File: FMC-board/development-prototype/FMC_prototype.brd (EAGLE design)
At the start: 103.8 x 69.8 mm, 72 parts, among them J1 DC_POWER_JACK-PJ-102AH, J2 DC_POWER_JACK-PJ-102AH

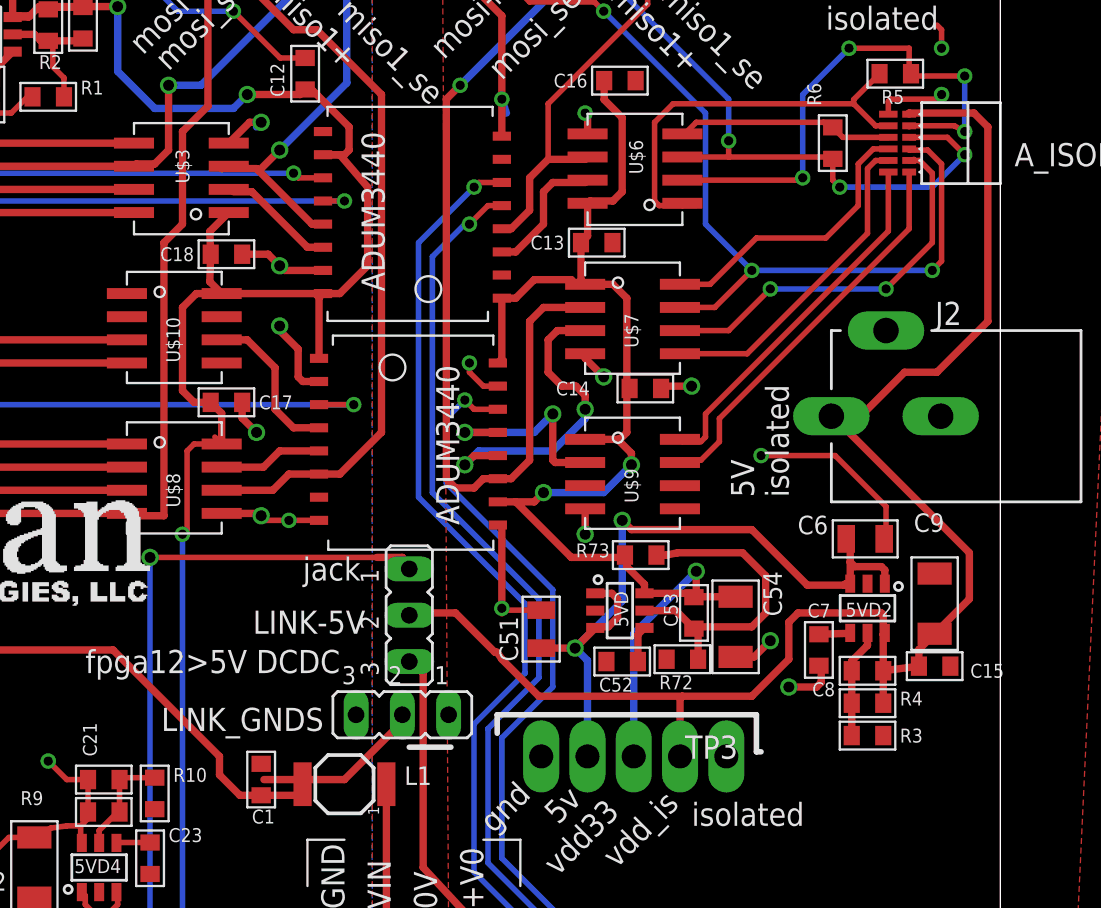
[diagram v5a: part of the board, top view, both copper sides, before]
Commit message: Fixed small routing error on DC DC converter
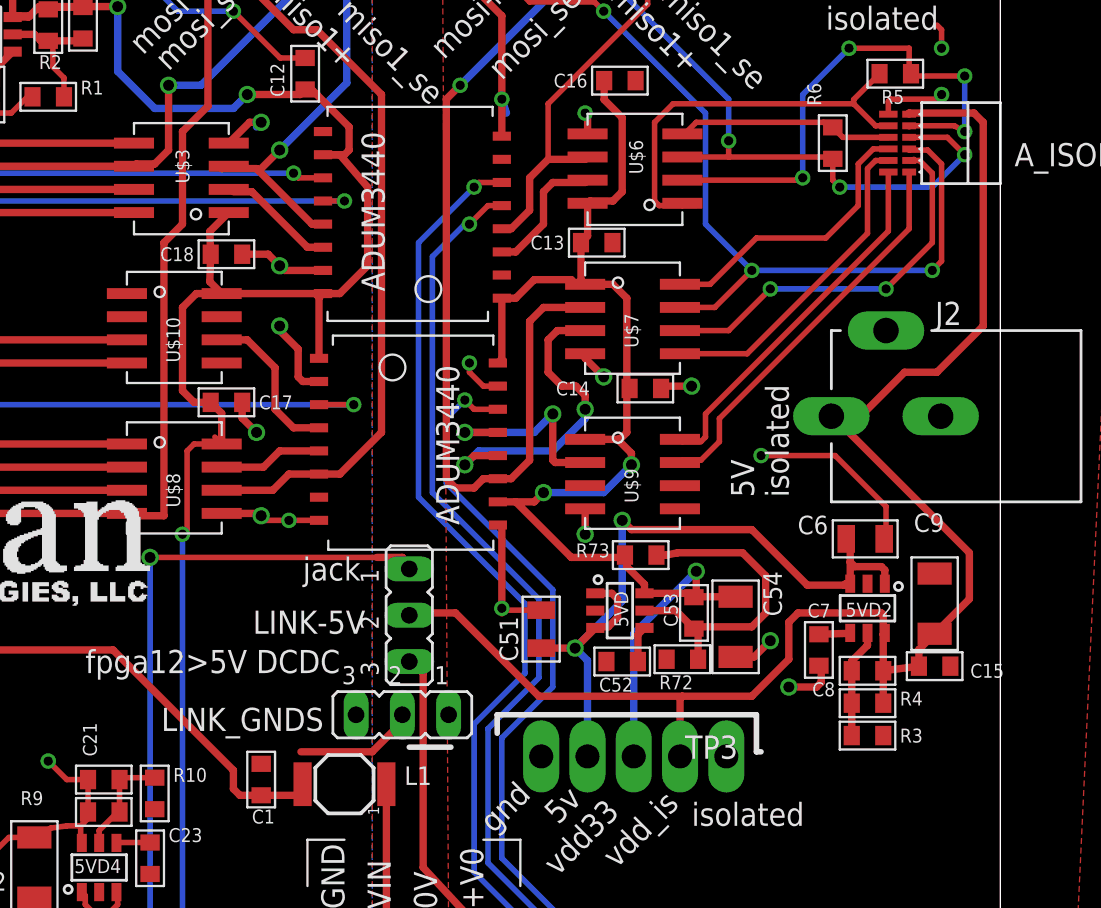
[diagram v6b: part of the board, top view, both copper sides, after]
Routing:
- net GND: track 104.7 -> 102.0 mm
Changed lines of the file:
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@@
 <grid distance="0.01" unitdist="inch" unit="inch" style="lines" multiple="1" display="yes" altdistance="0.0125" altunitdist="inch" altunit="inch"/>
 <layers>
-<layer number="1" name="Top" color="12" fill="1" visible="no" active="yes"/>
+<layer number="1" name="Top" color="12" fill="1" visible="yes" active="yes"/>
 <layer number="2" name="$GND" color="2" fill="1" visible="no" active="yes"/>
 <layer number="3" name="Route3" color="4" fill="3" visible="no" active="no"/>
@@
 <contactref element="U$20" pad="P1"/>
 <wire x1="70.993" y1="25.146" x2="70.993" y2="24.765" width="0.4064" layer="1"/>
-<wire x1="70.993" y1="24.765" x2="67.818" y2="21.59" width="0.4064" layer="1"/>
-<wire x1="67.818" y1="21.59" x2="63.3984" y2="21.59" width="0.4064" layer="1"/>
+<wire x1="70.993" y1="24.765" x2="69.342" y2="23.114" width="0.4064" layer="1"/>
+<wire x1="69.342" y1="23.114" x2="65.4304" y2="23.114" width="0.4064" layer="1"/>
 <wire x1="15.24" y1="57.15" x2="15.24" y2="54.61" width="0" layer="19" extent="16-16"/>
 <wire x1="21.59" y1="35.56" x2="21.59" y2="39.37" width="0" layer="19" extent="16-16"/>
@@
 <wire x1="90.17" y1="26.162" x2="86.36" y2="26.162" width="0.4064" layer="1"/>
 <wire x1="86.36" y1="26.162" x2="78.486" y2="26.162" width="0.4064" layer="1"/>
-<wire x1="78.486" y1="26.162" x2="76.454" y2="28.194" width="0.4064" layer="1"/>
-<wire x1="76.454" y1="28.194" x2="76.2" y2="28.575" width="0.4064" layer="1"/>
 <wire x1="94.536" y1="41.529" x2="94.615" y2="41.529" width="0.4064" layer="1"/>
 <wire x1="94.615" y1="41.529" x2="102.108" y2="34.036" width="0.4064" layer="1"/>
@@
 <wire x1="96.139" y1="41.529" x2="98.552" y2="43.942" width="0.4064" layer="1"/>
 <wire x1="98.552" y1="43.942" x2="100.33" y2="43.942" width="0.4064" layer="1"/>
-<wire x1="100.33" y1="43.942" x2="103.124" y2="46.736" width="0.4064" layer="1"/>
-<wire x1="103.124" y1="46.736" x2="103.124" y2="57.404" width="0.4064" layer="1"/>
-<wire x1="103.124" y1="57.404" x2="102.362" y2="58.166" width="0.4064" layer="1"/>
+<wire x1="100.33" y1="43.942" x2="102.87" y2="46.482" width="0.4064" layer="1"/>
+<wire x1="102.87" y1="46.482" x2="102.87" y2="57.658" width="0.4064" layer="1"/>
+<wire x1="102.87" y1="57.658" x2="102.362" y2="58.166" width="0.4064" layer="1"/>
 <wire x1="102.362" y1="58.166" x2="98.806" y2="58.166" width="0.4064" layer="1"/>
 <wire x1="98.806" y1="58.166" x2="98.806" y2="58.1025" width="0.4064" layer="1"/>
@@
 <wire x1="86.233" y1="26.035" x2="86.36" y2="26.162" width="0.4064" layer="1"/>
 <contactref element="LINK-5V" pad="2"/>
-<wire x1="76.2" y1="28.575" x2="76.073" y2="28.575" width="0.4064" layer="1"/>
-<wire x1="76.073" y1="28.575" x2="73.914" y2="30.734" width="0.4064" layer="1"/>
 <wire x1="73.914" y1="30.734" x2="71.501" y2="30.734" width="0.4064" layer="1"/>
 <wire x1="71.501" y1="30.734" x2="71.374" y2="30.607" width="0.4064" layer="1"/>
+<wire x1="78.486" y1="26.162" x2="73.914" y2="30.734" width="0.4064" layer="1"/>
 </signal>
 <signal name="VDD33">
@@
 <wire x1="65.518" y1="21.096" x2="65.532" y2="21.082" width="0.4064" layer="1"/>
 <wire x1="63.246" y1="20.7264" x2="62.0776" y2="20.7264" width="0.4064" layer="1"/>
-<wire x1="62.0776" y1="20.7264" x2="60.96" y2="21.844" width="0.4064" layer="1"/>
-<wire x1="60.96" y1="21.844" x2="60.96" y2="22.86" width="0.4064" layer="1"/>
-<wire x1="60.96" y1="22.86" x2="55.118" y2="28.702" width="0.4064" layer="1"/>
+<wire x1="62.0776" y1="20.7264" x2="61.722" y2="21.082" width="0.4064" layer="1"/>
+<wire x1="61.722" y1="21.082" x2="61.722" y2="22.098" width="0.4064" layer="1"/>
+<wire x1="61.722" y1="22.098" x2="55.118" y2="28.702" width="0.4064" layer="1"/>
 <wire x1="55.118" y1="28.702" x2="43.688" y2="28.702" width="0.4064" layer="1"/>
 <wire x1="43.688" y1="28.702" x2="42.164" y2="30.226" width="0.4064" layer="1"/>

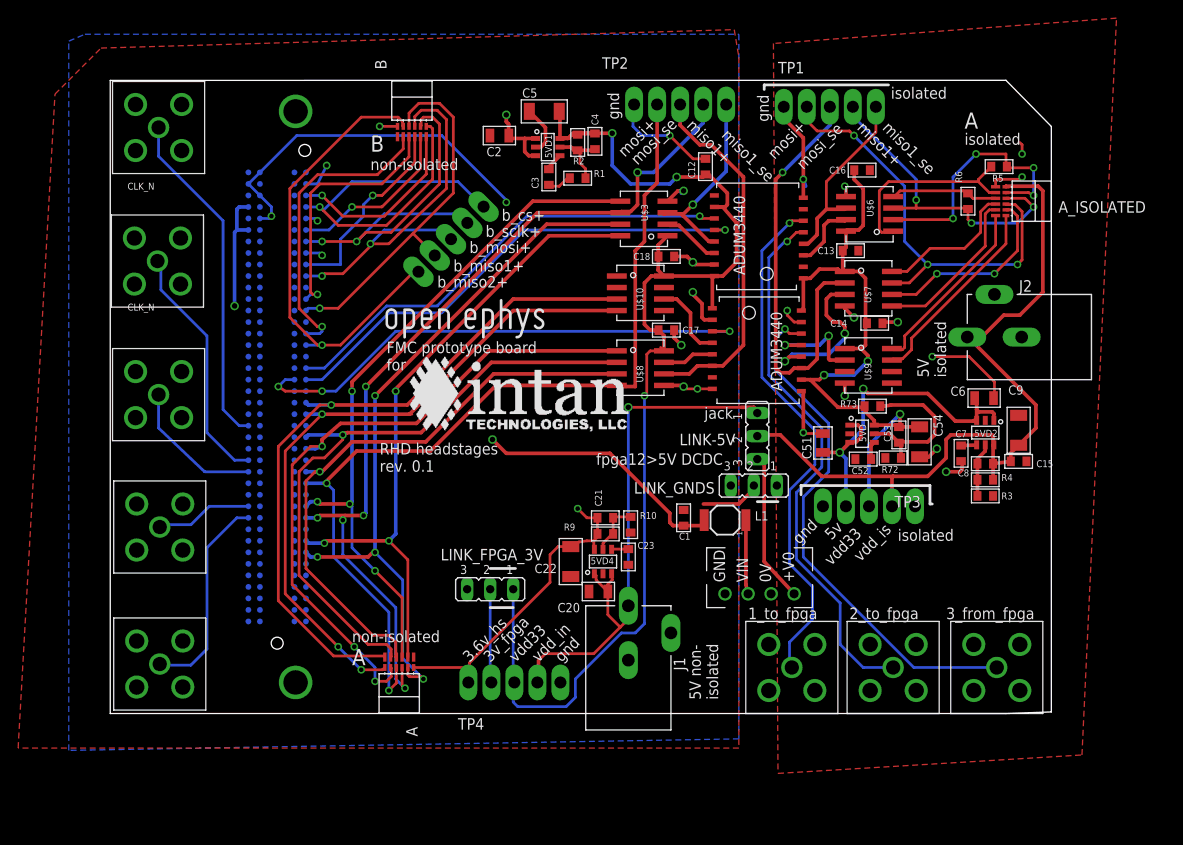
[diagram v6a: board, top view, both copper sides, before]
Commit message: Cleaning up schematic as a means to understand and verify it.
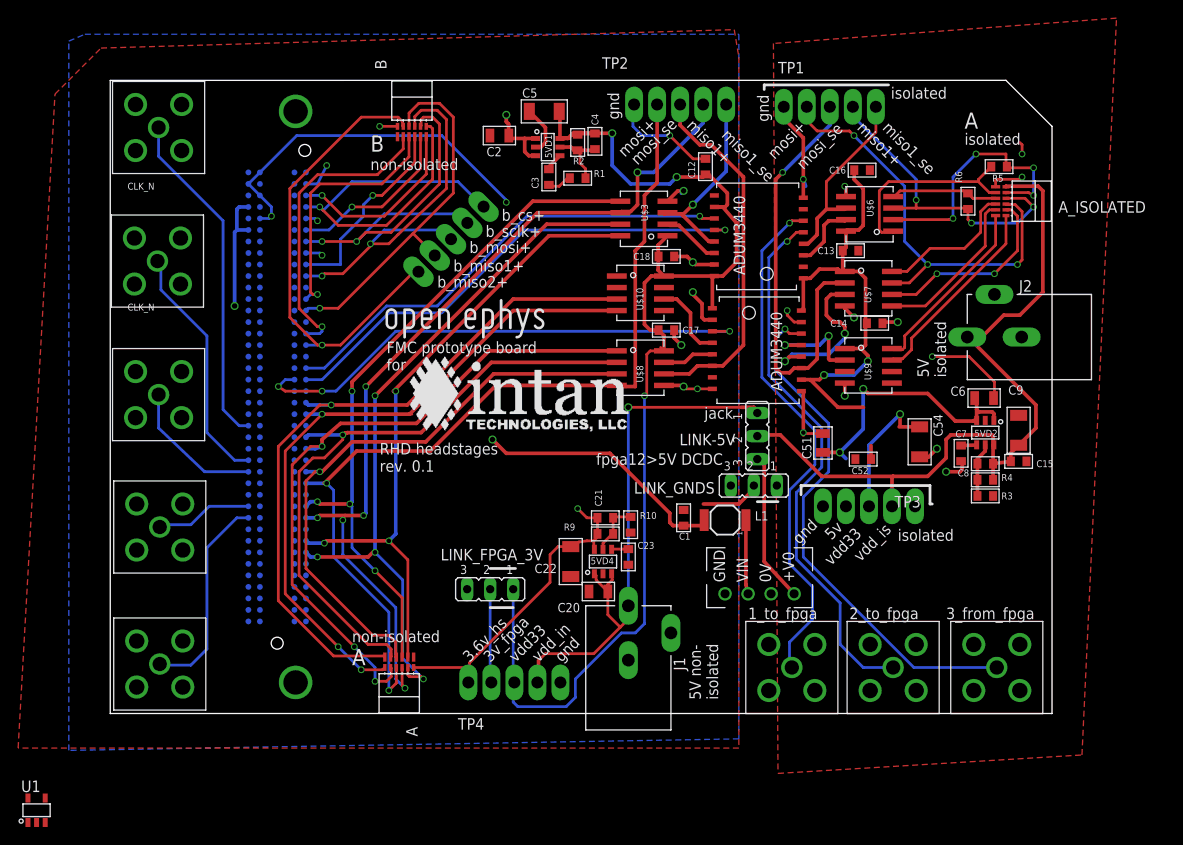
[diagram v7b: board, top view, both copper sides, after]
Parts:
- removed 5VD: TPS79301, RHD2000_eval_board:SOT-23-6
- removed C53: 15p, RHD2000_eval_board:0603
- removed R72: 30.9k, RHD2000_eval_board:0603
- removed R73: 95.3k, RHD2000_eval_board:0603
- added U1: TPS79333, jonnew:SOT-23-5
- J2: value DC_POWER_JACK-PJ-102AH -> PJ-102AH
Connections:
- net VDD33 renamed +3V3
- net VDD36 renamed +3V6
- net VDD_ISOLATED renamed VDD_ISO
- removed net GND_ISOLATED: 5VD.2, 5VD2.2, A_ISOLATED.T6, C13.2, C14.2, C15.2, C16.2, C51.2, C52.2, C54.2, C6.2, C7.2, C9.2, J2.2, J2.3, LINK_GNDS.1, R3.2, R72.2, TP1.TP-1, TP3.TP-1, TP3.TP-5, U$11.P2, U$11.P8, U$12.P15, U$12.P9, U$17.GND$1, U$17.GND$2, U$17.GND$3, U$17.GND$4, U$18.GND$1, U$18.GND$2, U$18.GND$3, U$18.GND$4, U$19.GND$1, U$19.GND$2, U$19.GND$3, U$19.GND$4, U$20.P3, U$6.P5, U$7.P4, U$9.P4
- removed net N$108: 5VD.5, C53.2, R72.1, R73.1
- removed net N$3: LINK_FPGA_3V.3
- removed net VDD33_ISOLATED: 5VD.6, C13.1, C14.1, C16.1, C53.1, C54.1, R73.2, TP3.TP-3, U$11.P1, U$12.P10, U$12.P16, U$6.P8, U$7.P1, U$9.P1
- new net 5V_ISO: TP3.TP-4
- new net GND_ISO: 5VD2.2, A_ISOLATED.T6, C13.2, C14.2, C15.2, C16.2, C51.2, C52.2, C54.2, C6.2, C7.2, C9.2, J2.2, J2.3, LINK_GNDS.1, R3.2, TP1.TP-1, TP3.TP-1, TP3.TP-5, U$11.P2, U$11.P8, U$12.P15, U$12.P9, U$17.GND$1, U$17.GND$2, U$17.GND$3, U$17.GND$4, U$18.GND$1, U$18.GND$2, U$18.GND$3, U$18.GND$4, U$19.GND$1, U$19.GND$2, U$19.GND$3, U$19.GND$4, U$20.P3, U$6.P5, U$7.P4, U$9.P4, U1.2
- new net VDD33_ISO: C13.1, C14.1, C16.1, C54.1, TP3.TP-3, U$11.P1, U$12.P10, U$12.P16, U$6.P8, U$7.P1, U$9.P1, U1.5
- net 5V_ISOLATED: now also U1.1, U1.3; no longer 5VD.1, 5VD.3, TP3.TP-4
- net GND: now also U$4.P$6
- net N$97: now also U1.4; no longer 5VD.4
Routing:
- net VDD33_ISOLATED: track 72.0 -> 0.00 mm, vias 3 -> 0
- net VDD33_ISO: track 0.00 -> 66.3 mm, vias 0 -> 3
- net GND_ISOLATED: track 48.6 -> 0.00 mm, vias 12 -> 0
- net GND_ISO: track 0.00 -> 48.6 mm, vias 0 -> 12
- net N$108: track 17.8 -> 0.00 mm
- net 5V_ISOLATED: track 41.0 -> 30.3 mm
- net N$97: track 1.99 -> 1.48 mm
- added copper zone on layer 1, net GND_ISO
- added copper zone on layer 2, net GND_ISO
- removed copper zone on layer 1, net GND_ISOLATED
- removed copper zone on layer 2, net GND_ISOLATED
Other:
- board size 103.8 x 69.8 mm -> 103.9 x 69.8 mm

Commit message: Looks like isolated 5V was wired to output of isolated 3.6V regulator and input is floating to both isolated regulators. In the middle of fixing that.
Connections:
- removed net VDD_ISO: 5VD2.6, A_ISOLATED.B6, C15.1, C8.1, C9.1, J2.1, LINK-5V.2, R4.2, TP3.TP-2
- new net +3V6_ISO: 5VD2.6, A_ISOLATED.B6, C15.1, C8.1, C9.1, R4.2, TP3.TP-2
- new net N$3: C51.2, C52.2, C54.2, U1.2
- new net N$4: J2.2, J2.3, LINK_GNDS.1
- new net N$5: J2.1, LINK-5V.2
- net GND_ISO: no longer C51.2, C52.2, C54.2, J2.2, J2.3, LINK_GNDS.1, U1.2
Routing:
- net VDD_ISO: track 85.2 -> 0.00 mm
- net +3V6_ISO: track 0.00 -> 85.0 mm
- net GND_ISO: track 48.6 -> 44.1 mm, vias 12 -> 10
- net N$3: track 0.00 -> 4.47 mm, vias 0 -> 2
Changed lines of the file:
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@@
 <contactref element="C14" pad="2"/>
 <contactref element="C13" pad="2"/>
-<contactref element="C51" pad="2"/>
-<contactref element="C52" pad="2"/>
-<contactref element="C54" pad="2"/>
 <contactref element="5VD2" pad="2"/>
 <contactref element="C6" pad="2"/>
@@
 <contactref element="TP1" pad="TP-1"/>
 <contactref element="TP3" pad="TP-1"/>
-<contactref element="J2" pad="3"/>
-<contactref element="J2" pad="2"/>
-<contactref element="LINK_GNDS" pad="1"/>
 <polygon width="0.4064" layer="1">
 <vertex x="73.152" y="73.914"/>
@@
 <wire x1="86.868" y1="43.18" x2="85.3186" y2="43.18" width="0.4064" layer="1"/>
 <wire x1="85.3186" y1="43.18" x2="85.1916" y2="43.053" width="0.4064" layer="1"/>
-<wire x1="89.281" y1="28.321" x2="90.297" y2="28.321" width="0.4064" layer="1"/>
-<wire x1="90.297" y1="28.321" x2="91.186" y2="29.21" width="0.4064" layer="1"/>
-<via x="91.186" y="29.21" extent="1-16" drill="0.6"/>
 <via x="92.202" y="26.67" extent="1-16" drill="0.6"/>
 <wire x1="92.202" y1="26.67" x2="93.726" y2="26.67" width="0.4064" layer="1"/>
@@
 <wire x1="97.536" y1="36.576" x2="97.536" y2="34.8996" width="0.3048" layer="1"/>
 <wire x1="97.536" y1="34.8996" x2="97.4344" y2="34.798" width="0.3048" layer="1"/>
-<wire x1="78.613" y1="30.8864" x2="76.5556" y2="30.8864" width="0.3048" layer="1"/>
-<wire x1="76.5556" y1="30.8864" x2="76.454" y2="30.988" width="0.3048" layer="1"/>
-<via x="76.454" y="30.988" extent="1-16" drill="0.5"/>
 <polygon width="0.4064" layer="2">
 <vertex x="72.644" y="71.882"/>
@@
 <contactref element="C15" pad="2"/>
 <contactref element="U$20" pad="P3"/>
-<contactref element="U1" pad="2"/>
-<wire x1="72.644" y1="2.54" x2="-8.128" y2="-12.018" width="0" layer="19" extent="1-1"/>
-</signal>
-<signal name="VDD_ISO">
+</signal>
+<signal name="+3V6_ISO">
 <contactref element="C15" pad="1"/>
 <contactref element="A_ISOLATED" pad="B6"/>
@@
 <contactref element="R4" pad="2"/>
 <contactref element="TP3" pad="TP-2"/>
-<contactref element="J2" pad="1"/>
 <wire x1="97.3836" y1="25.781" x2="97.3836" y2="27.559" width="0.4064" layer="1"/>
 <wire x1="97.3836" y1="27.559" x2="97.3836" y2="29.5516" width="0.4064" layer="1"/>
@@
 <wire x1="90.17" y1="26.162" x2="86.36" y2="26.162" width="0.4064" layer="1"/>
 <wire x1="86.36" y1="26.162" x2="78.486" y2="26.162" width="0.4064" layer="1"/>
-<wire x1="94.536" y1="41.529" x2="94.615" y2="41.529" width="0.4064" layer="1"/>
 <wire x1="94.615" y1="41.529" x2="102.108" y2="34.036" width="0.4064" layer="1"/>
 <wire x1="102.108" y1="34.036" x2="102.108" y2="31.496" width="0.4064" layer="1"/>
@@
 <wire x1="86.233" y1="22.86" x2="86.233" y2="26.035" width="0.4064" layer="1"/>
 <wire x1="86.233" y1="26.035" x2="86.36" y2="26.162" width="0.4064" layer="1"/>
-<contactref element="LINK-5V" pad="2"/>
 <wire x1="73.914" y1="30.734" x2="71.501" y2="30.734" width="0.4064" layer="1"/>
-<wire x1="71.501" y1="30.734" x2="71.374" y2="30.607" width="0.4064" layer="1"/>
 <wire x1="78.486" y1="26.162" x2="73.914" y2="30.734" width="0.4064" layer="1"/>
 </signal>
@@
 <contactref element="TP3" pad="TP-4"/>
 </signal>
+<signal name="N$3">
+<contactref element="C51" pad="2"/>
+<contactref element="C52" pad="2"/>
+<contactref element="C54" pad="2"/>
+<contactref element="U1" pad="2"/>
+<wire x1="89.281" y1="28.321" x2="90.297" y2="28.321" width="0.4064" layer="1"/>
+<wire x1="90.297" y1="28.321" x2="91.186" y2="29.21" width="0.4064" layer="1"/>
+<via x="91.186" y="29.21" extent="1-16" drill="0.6"/>
+<wire x1="78.613" y1="30.8864" x2="76.5556" y2="30.8864" width="0.3048" layer="1"/>
+<wire x1="76.5556" y1="30.8864" x2="76.454" y2="30.988" width="0.3048" layer="1"/>
+<via x="76.454" y="30.988" extent="1-16" drill="0.5"/>
+<wire x1="82.1944" y1="28.067" x2="89.281" y2="28.321" width="0" layer="19" extent="1-1"/>
+<wire x1="78.613" y1="30.8864" x2="82.1944" y2="28.067" width="0" layer="19" extent="1-1"/>
+<wire x1="-8.128" y1="-12.018" x2="76.454" y2="30.988" width="0" layer="19" extent="1-1"/>
+</signal>
+<signal name="N$4">
+<contactref element="J2" pad="3"/>
+<contactref element="J2" pad="2"/>
+<contactref element="LINK_GNDS" pad="1"/>
+<wire x1="100.536" y1="41.529" x2="97.536" y2="46.229" width="0" layer="19" extent="1-1"/>
+<wire x1="73.533" y1="25.146" x2="100.536" y2="41.529" width="0" layer="19" extent="1-1"/>
+</signal>
+<signal name="N$5">
+<contactref element="J2" pad="1"/>
+<contactref element="LINK-5V" pad="2"/>
+<wire x1="71.374" y1="30.607" x2="94.536" y2="41.529" width="0" layer="19" extent="1-1"/>
+</signal>
 </signals>
